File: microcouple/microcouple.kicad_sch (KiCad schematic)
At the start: 1 part, among them P1 USB_C_Plug

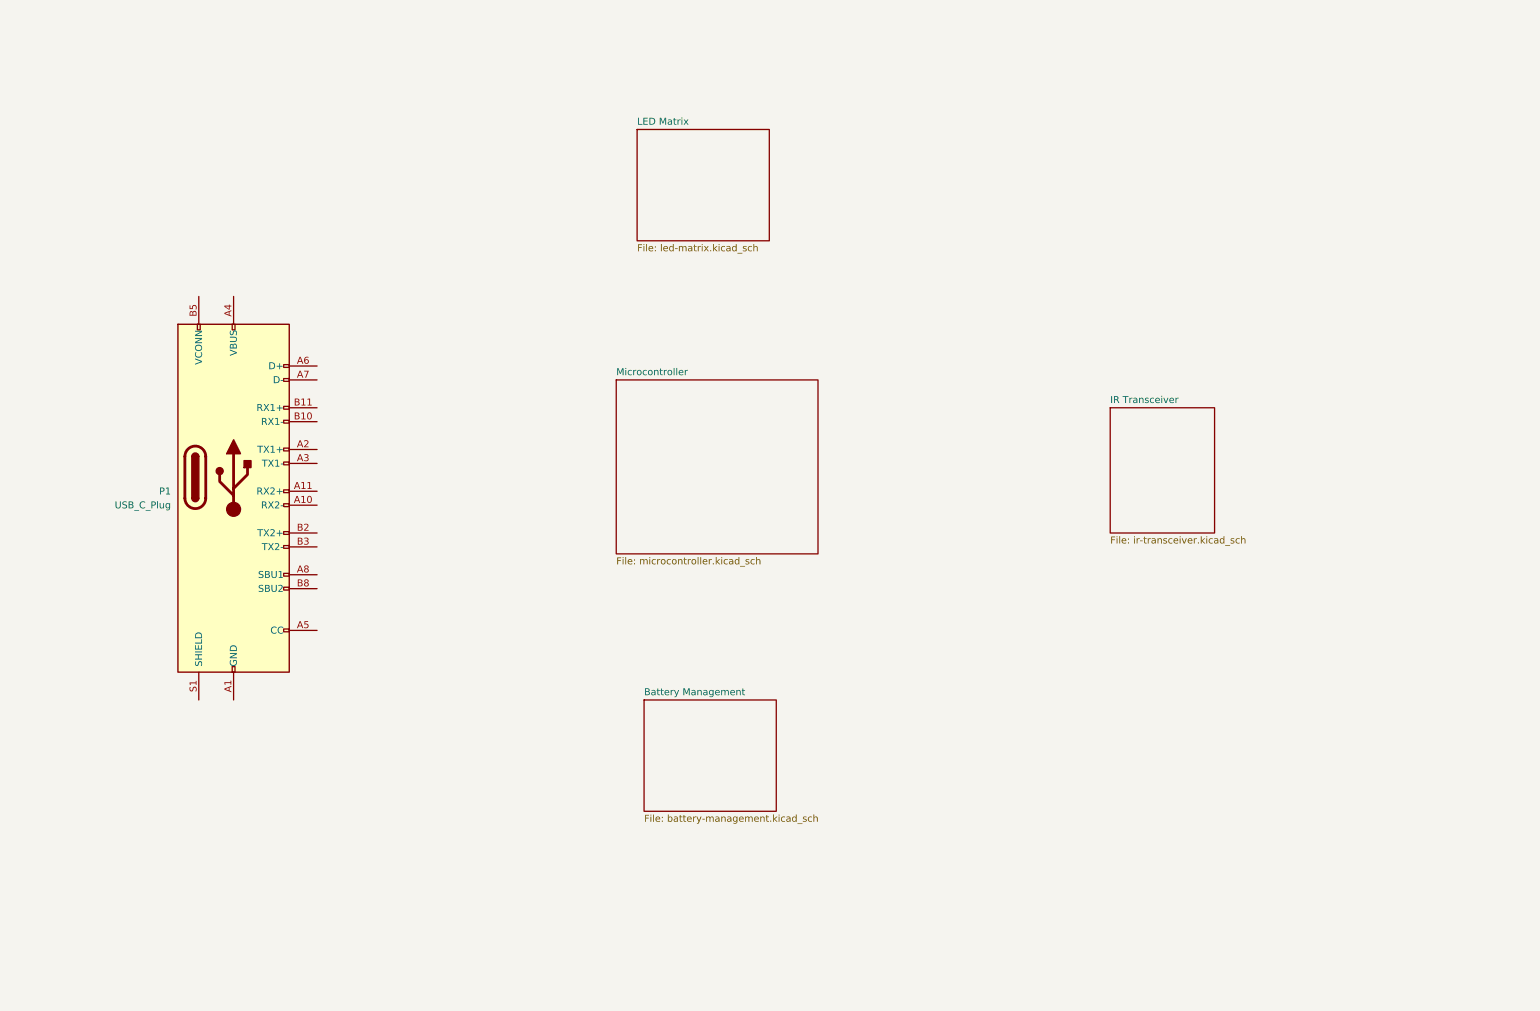
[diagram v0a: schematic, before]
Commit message: Add decoupling caps on MCU
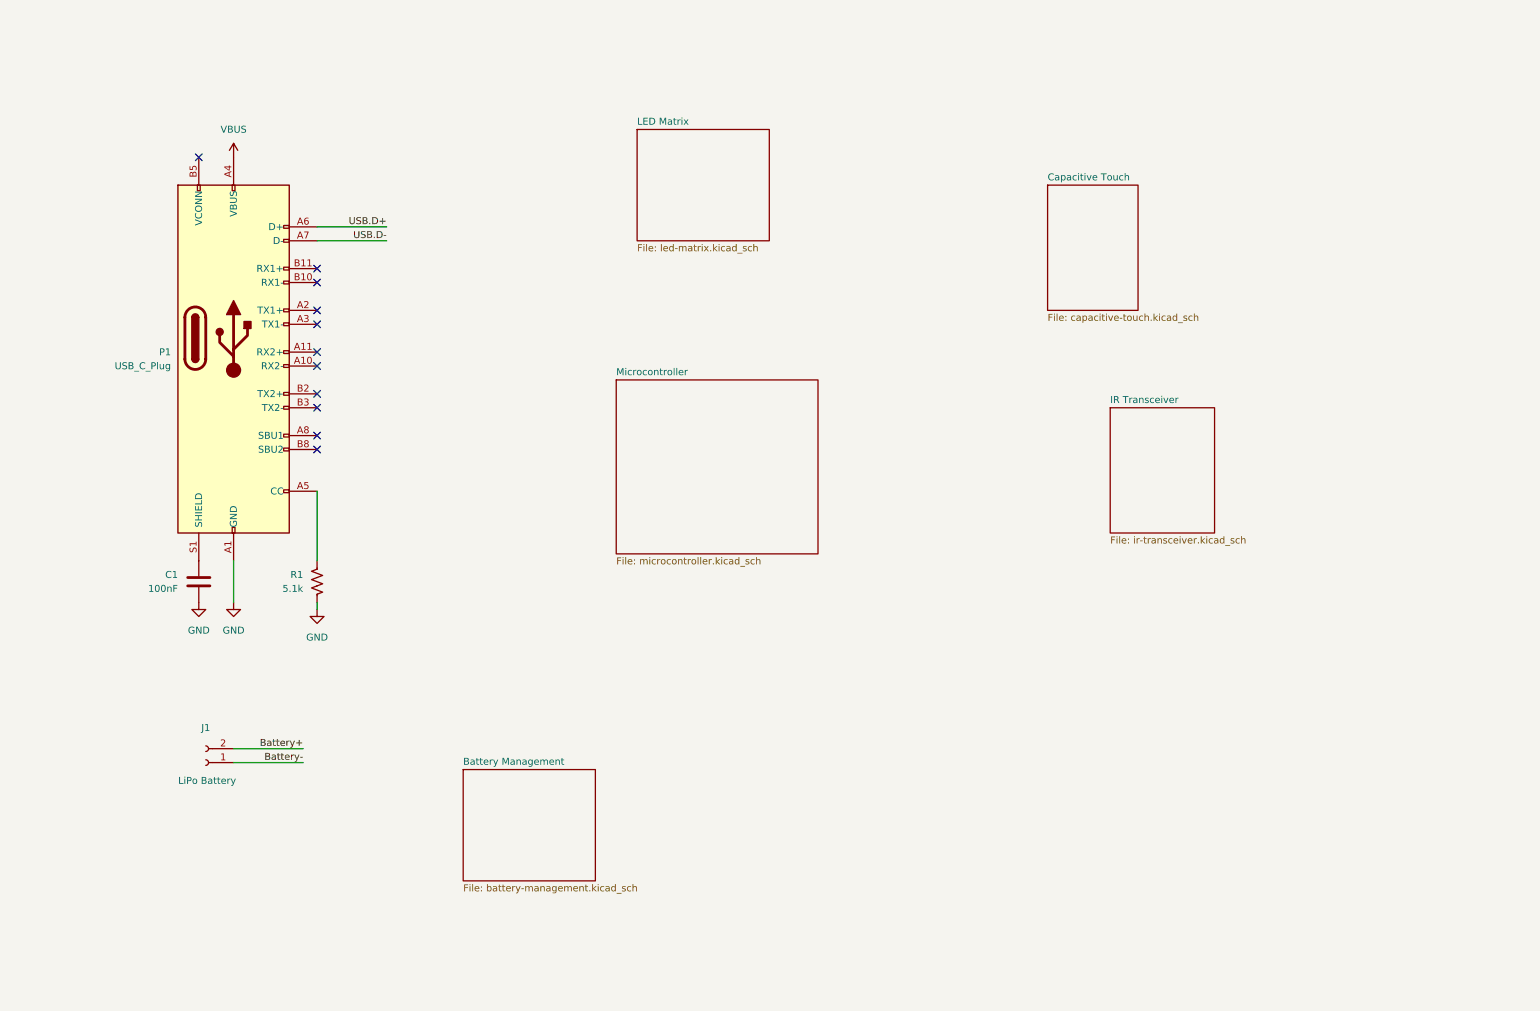
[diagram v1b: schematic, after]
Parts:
- added C1: 100nF, Capacitor_SMD:C_0805_2012Metric, symbol Device:C
- added J1: LiPo Battery, Connector_JST:JST_PH_S2B-PH-K_1x02_P2.00mm_Horizontal, symbol Connector:Conn_01x02_Socket
- added R1: 5.1k, Resistor_SMD:R_0805_2012Metric_Pad1.20x1.40mm_HandSolder, symbol Device:R_US
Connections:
- net GND: now reaches P1.A1 (GND), P1.A12 (GND), P1.B1 (GND), P1.B12 (GND)
- net GND: now also C1.2, R1.2
- net VBUS: now reaches P1.A4 (VBUS), P1.A9 (VBUS), P1.B4 (VBUS), P1.B9 (VBUS)
- net at P1.A5 (CC): now also R1.1
- net USB.D+: now reaches P1.A6 (D+)
- net USB.D-: now reaches P1.A7 (D-)
- net at P1.S1 (SHIELD): now also C1.1
- new net Battery+: J1.2 (Pin_2)
- new net Battery-: J1.1 (Pin_1)
- no-connect marks 0 -> 11
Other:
- added sheet Capacitive Touch (capacitive-touch.kicad_sch)
- moved on the sheet: P1

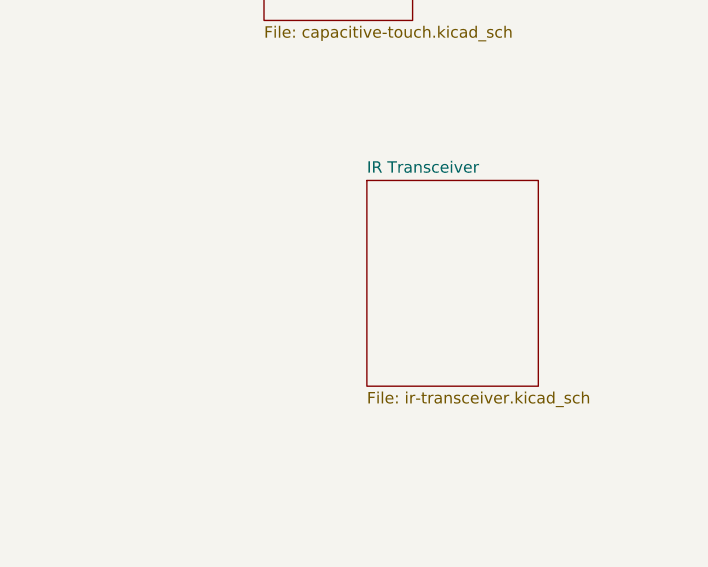
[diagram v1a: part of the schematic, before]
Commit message: Sketch out LED matrix
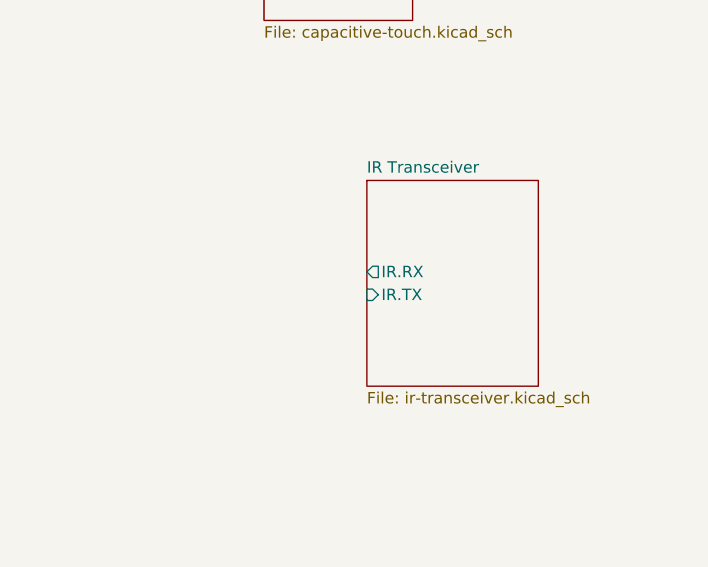
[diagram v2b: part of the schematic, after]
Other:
- sheet IR Transceiver ports: added IR.RX, IR.TX; removed none
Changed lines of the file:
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@@
+			)
+		)
+		(pin "IR.RX" output
+			(at 213.36 96.52 180)
+			(effects
+				(font
+					(size 1.27 1.27)
+				)
+				(justify left)
+			)
+		)
+		(pin "IR.TX" input
+			(at 213.36 99.06 180)
+			(effects
+				(font
+					(size 1.27 1.27)
+				)
+				(justify left)
 			)
 		)

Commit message: Finalize battery management
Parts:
- removed J1: LiPo Battery, Connector_JST:JST_PH_S2B-PH-K_1x02_P2.00mm_Horizontal, symbol Connector:Conn_01x02_Socket
- added BT1: 3.7V Lipo battery, Connector_JST:JST_PH_S2B-PH-K_1x02_P2.00mm_Horizontal, symbol Device:Battery_Cell
- added C15, C8, C9: 4.7uF, Capacitor_SMD:C_0805_2012Metric_Pad1.18x1.45mm_HandSolder, symbol Device:C
- added C2, C3, C4, C5, C6, C7: 100nF, Capacitor_SMD:C_0805_2012Metric_Pad1.18x1.45mm_HandSolder, symbol Device:C
- added D69: IR, LED_THT:LED_D5.0mm_Horizontal_O1.27mm_Z3.0mm_Clear, symbol Device:LED
- added FB1: 120R @ 100MHz, Inductor_SMD:L_0805_2012Metric_Pad1.15x1.40mm_HandSolder, symbol Device:FerriteBead
- added R7: 180R, Resistor_SMD:R_0805_2012Metric_Pad1.20x1.40mm_HandSolder, symbol Device:R_US
- added U1: RP2040, Package_DFN_QFN:QFN-56-1EP_7x7mm_P0.4mm_EP3.2x3.2mm, symbol MCU_RaspberryPi:RP2040
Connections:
- net GND: now also BT1.2 (-), C15.2, C2.2, C4.2, C5.2, C6.2, C7.2, C8.2, C9.2, U1.57 (GND)
- net VBUS: now also C15.1
- new net: U1.1 (IOVDD), U1.10 (IOVDD), U1.22 (IOVDD), U1.33 (IOVDD), U1.42 (IOVDD), U1.49 (IOVDD)
- new net: U1.23 (DVDD), U1.50 (DVDD)
- new net +3.3V: C2.1, C3.1, C4.1, C5.1, C6.1, C8.1, FB1.1
- new net +3.3VA: C7.1, C9.1, FB1.2
- new net Battery Management/BATT+: BT1.1 (+)
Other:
- removed sheet Microcontroller
- sheet Battery Management ports: added +3.3V, BATT+, VBUS; removed none
- note added: "Modulated at 38kHz NEC transmission protocol"
- moved on the sheet: C1, P1, R1

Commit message: Finish base MCU design
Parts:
- added C10: 100nF, Capacitor_SMD:C_0805_2012Metric_Pad1.18x1.45mm_HandSolder, symbol Device:C
- added C11: 4.7uF, Capacitor_SMD:C_0805_2012Metric_Pad1.18x1.45mm_HandSolder, symbol Device:C
- added J1: Conn_ARM_SWD_TagConnect_TC2030-NL, Connector:Tag-Connect_TC2030-IDC-NL_2x03_P1.27mm_Vertical, symbol Connector:Conn_ARM_SWD_TagConnect_TC2030-NL
- added R2: 5.1k, Resistor_SMD:R_0805_2012Metric_Pad1.20x1.40mm_HandSolder, symbol Device:R_US
- added SW1: ~{RESET}, Button_Switch_SMD:SW_SPST_PTS810, symbol Switch:SW_Push
- added X1: 12 MHz 12 pF, Crystal:Crystal_SMD_3225-4Pin_3.2x2.5mm_HandSoldering, symbol Device:Crystal_GND24
- BT1: value 3.7V Lipo battery -> 3.7 V LiPo
- C2, C3: value 100nF -> 14 pF
- P1: footprint GS_Connectors:USB-C-SMD -> (none)
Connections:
- net +3.3V: now also U1.1 (IOVDD), U1.10 (IOVDD), U1.22 (IOVDD), U1.33 (IOVDD), U1.42 (IOVDD), U1.44 (VREG_IN), U1.48 (USB_VDD), U1.49 (IOVDD), J1.1 (VCC), R2.1; no longer C2.1, C3.1
- net +3.3VA: now also U1.43 (ADC_AVDD)
- net GND: now also C3.2, U1.19 (TESTEN), C10.2, C11.2, J1.5 (GND), SW1.1, X1.2, X1.4
- net USB.D+: now also U1.47 (USB_DP)
- net USB.D-: now also U1.46 (USB_DM)
- net XIN: now reaches U1.20 (XIN)
- net XIN: now also C3.1, X1.1
- net XOUT: now reaches U1.21 (XOUT)
- net XOUT: now also C2.1, X1.3
- net +1V1: now reaches U1.23 (DVDD), U1.50 (DVDD)
- net +1V1: now also U1.45 (VREG_VOUT), C10.1, C11.1
- net SWCLK: now reaches U1.24 (SWCLK)
- net SWCLK: now also J1.4 (SWCLK)
- net SWDIO: now reaches U1.25 (SWD)
- net SWDIO: now also J1.2 (SWDIO)
- net ~{RESET}: now reaches U1.26 (RUN)
- net ~{RESET}: now also J1.3 (~{RESET}), R2.2, SW1.2
- no-connect marks 11 -> 12
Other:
- removed sheet IR Transceiver
- moved on the sheet: BT1, C1, C15, C4, C5, C6, C7, C8, C9, D69, FB1, P1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

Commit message: Preliminary Schematic
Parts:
- removed R7: 180R, Resistor_SMD:R_0805_2012Metric_Pad1.20x1.40mm_HandSolder, symbol Device:R_US
- added R10, R9: 5.1k, Resistor_SMD:R_0201_0603Metric, symbol Device:R_US
- added R15, R16: 27R, Resistor_SMD:R_0201_0603Metric, symbol Device:R_US
- added R8: 1k, Resistor_SMD:R_0201_0603Metric, symbol Device:R_US
- added U7: USBLC6-2SC6, Package_TO_SOT_SMD:SOT-23-6, symbol Power_Protection:USBLC6-2SC6
- BT1: value 3.7 V LiPo -> 3.7V LiPo
- C1: renamed from C8; footprint Capacitor_SMD:C_0805_2012Metric_Pad1.18x1.45mm_HandSolder -> Capacitor_SMD:C_0402_1005Metric
- C10: renamed from C3; footprint Capacitor_SMD:C_0805_2012Metric_Pad1.18x1.45mm_HandSolder -> Capacitor_SMD:C_0201_0603Metric
- C11: renamed from C2; footprint Capacitor_SMD:C_0805_2012Metric_Pad1.18x1.45mm_HandSolder -> Capacitor_SMD:C_0201_0603Metric
- C12: renamed from C1; footprint Capacitor_SMD:C_0805_2012Metric -> Capacitor_SMD:C_0201_0603Metric
- C2: renamed from C4; footprint Capacitor_SMD:C_0805_2012Metric_Pad1.18x1.45mm_HandSolder -> Capacitor_SMD:C_0201_0603Metric
- C3: renamed from C5; footprint Capacitor_SMD:C_0805_2012Metric_Pad1.18x1.45mm_HandSolder -> Capacitor_SMD:C_0201_0603Metric
- C4: renamed from C6; footprint Capacitor_SMD:C_0805_2012Metric_Pad1.18x1.45mm_HandSolder -> Capacitor_SMD:C_0201_0603Metric
- C5: renamed from C9; footprint Capacitor_SMD:C_0805_2012Metric_Pad1.18x1.45mm_HandSolder -> Capacitor_SMD:C_0402_1005Metric
- C6: renamed from C7; footprint Capacitor_SMD:C_0805_2012Metric_Pad1.18x1.45mm_HandSolder -> Capacitor_SMD:C_0201_0603Metric
- C7: renamed from C11; footprint Capacitor_SMD:C_0805_2012Metric_Pad1.18x1.45mm_HandSolder -> Capacitor_SMD:C_0402_1005Metric
- C8: renamed from C10; footprint Capacitor_SMD:C_0805_2012Metric_Pad1.18x1.45mm_HandSolder -> Capacitor_SMD:C_0201_0603Metric
- C9: renamed from C15; footprint Capacitor_SMD:C_0805_2012Metric_Pad1.18x1.45mm_HandSolder -> Capacitor_SMD:C_0402_1005Metric
- D69: value IR -> GREEN; footprint LED_THT:LED_D5.0mm_Horizontal_O1.27mm_Z3.0mm_Clear -> LED_SMD:LED_0201_0603Metric
- P1: footprint (none) -> GS_Connectors:USB-C-SMD
- R1: renamed from R2; footprint Resistor_SMD:R_0805_2012Metric_Pad1.20x1.40mm_HandSolder -> Resistor_SMD:R_0201_0603Metric
- R3: renamed from R1; footprint Resistor_SMD:R_0805_2012Metric_Pad1.20x1.40mm_HandSolder -> Resistor_SMD:R_0201_0603Metric
- X1: value 12 MHz 12 pF -> 12MHz 12pF
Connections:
- net +3.3V: now also D69.2 (A), R10.1, R9.1
- net GND: now also R8.2, U7.2 (GND)
- net USB.D+: now also U7.1 (I/O1); no longer U1.47 (USB_DP)
- net USB.D-: now also U7.3 (I/O2); no longer U1.46 (USB_DM)
- net VBUS: now also U7.5 (VBUS)
- net I2C0.SDA: now reaches U1.2 (GPIO0)
- net I2C0.SDA: now also R9.2
- net ~{MX_SDB}: now reaches U1.27 (GPIO16)
- net I2C0.SDL: now reaches U1.3 (GPIO1)
- net I2C0.SDL: now also R10.2
- net IR.TX: now reaches U1.37 (GPIO25)
- net IR.RX: now reaches U1.38 (GPIO26_ADC0)
- net CT_RESET: now reaches U1.5 (GPIO3)
- net CT_WAKE: now reaches U1.6 (GPIO4)
- net ~{CT_ALERT}: now reaches U1.7 (GPIO5)
- net at D69.1 (K): now also R8.1
- net Battery Management/BATT+ renamed +BATT
- new net: R16.2, U1.46 (USB_DM)
- new net: R15.2, U1.47 (USB_DP)
- new net USB.D_PROTECTED+: R15.1, U7.6 (I/O1)
- new net USB.D_PROTECTED-: R16.1, U7.4 (I/O2)
- no-connect marks 12 -> 40
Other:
- added sheet IR Transciever (ir-transciever.kicad_sch)
- sheet Battery Management ports: added +BATT; removed BATT+
- sheet Capacitive Touch ports: added CT_RESET, CT_WAKE, I2C.SCL, I2C.SDA, ~{CT_ALERT}; removed none
- sheet LED Matrix ports: added I2C.SCL, I2C.SDA, ~{MX_SDB}; removed none
- note removed: "Modulated at 38kHz NEC transmission protocol"
- company: (none) -> George Sleen
- moved on the sheet: BT1, C1, C2, C3, C4, C5, C6, C7, C8, C9, FB1, R1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

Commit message: Switch THT IR components to SMD ones
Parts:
- P1: LCSC ID C2835315 -> C2681555
- U2: renamed from U1; symbol MCU_RaspberryPi:RP2040 -> GS_MCU:RP2040
- X1: footprint Crystal:Crystal_SMD_3225-4Pin_3.2x2.5mm_HandSoldering -> Crystal:Crystal_SMD_3225-4Pin_3.2x2.5mm
- renumbered C4 to C1, C3 to C2, C2 to C3, C1 to C4, D69 to D1, R8 to R1, R1 to R2, R10 to R3, R9 to R4, R15 to R5, R16 to R6, R3 to R7, U7 to U1
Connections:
- net USB.D+: now also P1.B6 (D+)
- net USB.D-: now also P1.B7 (D-)
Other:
- moved on the sheet: BT1, C12, C9, D1, P1, R1, R2, R5, R6, R7, SW1, U1

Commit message: Fix faulty USB-C CC pin connections
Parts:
- added R17: 5.1k, Resistor_SMD:R_0201_0603Metric, symbol Device:R_US
- J1: renamed from P1; value USB_C_Plug -> USB_C_Socket; symbol GS_Connectors:USB_C_Plug -> GS_Connectors:USB_C_Socket
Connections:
- net GND: now also R17.1
- net USB.D_PROTECTED-: now also R6.2; no longer R6.1
- net at U2.46 (USB_DM): now also R6.1; no longer R6.2
- net at J1.A5 (CC1): now also R17.2; no longer R7.1
- net at J1.B5 (CC2): now also R7.1
- no-connect marks 40 -> 39
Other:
- moved on the sheet: R6
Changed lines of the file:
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@@
 	)
 	(no_connect
-		(at 39.37 66.04)
-	)
-	(no_connect
 		(at 185.42 121.92)
 	)
@@
 	(wire
 		(pts
+			(xy 67.31 139.7) (xy 67.31 124.46)
+		)
+		(stroke
+			(width 0)
+			(type default)
+		)
+	)
+	(wire
+		(pts
+			(xy 67.31 124.46) (xy 60.96 124.46)
+		)
+		(stroke
+			(width 0)
+			(type default)
+		)
+	)
+	(wire
+		(pts
 			(xy 92.71 116.84) (xy 85.09 116.84)
 		)
@@
 	(wire
 		(pts
+			(xy 67.31 148.59) (xy 67.31 147.32)
+		)
+		(stroke
+			(width 0)
+			(type default)
+		)
+	)
+	(wire
+		(pts
 			(xy 83.82 81.28) (xy 115.57 81.28)
 		)
@@
 	)
 	(symbol
+		(lib_id "Device:R_US")
+		(at 67.31 143.51 0)
+		(mirror x)
+		(unit 1)
+		(exclude_from_sim no)
+		(in_bom yes)
+		(on_board yes)
+		(dnp no)
+		(property "Reference" "R17"
+			(at 69.85 144.7801 0)
+			(effects
+				(font
+					(size 1.27 1.27)
+				)
+				(justify left)
+			)
+		)
+		(property "Value" "5.1k"
+			(at 69.85 142.2401 0)
+			(effects
+				(font
+					(size 1.27 1.27)
+				)
+				(justify left)
+			)
+		)
+		(property "Footprint" "Resistor_SMD:R_0201_0603Metric"
+			(at 68.326 143.256 90)
+			(effects
+				(font
+					(size 1.27 1.27)
+				)
+				(hide yes)
+			)
+		)
+		(property "Datasheet" "~"
+			(at 67.31 143.51 0)
+			(effects
+				(font
+					(size 1.27 1.27)
+				)
+				(hide yes)
+			)
+		)
+		(property "Description" "Resistor, US symbol"
+			(at 67.31 143.51 0)
+			(effects
+				(font
+					(size 1.27 1.27)
+				)
+				(hide yes)
+			)
+		)
+		(pin "1"
+		)
+		(pin "2"
+		)
+		(instances
+			(project "microcouple"
+				(path "/d639f16d-aedb-4af6-af94-94ea25244267"
+					(reference "R17")
+					(unit 1)
+				)
+			)
+		)
+	)
+	(symbol
 		(lib_id "Device:C")
 		(at 218.44 33.02 0)
@@
 	)
 	(symbol
-		(lib_id "GS_Connectors:USB_C_Plug")
+		(lib_id "GS_Connectors:USB_C_Socket")
 		(at 45.72 99.06 0)
 		(unit 1)
@@
 		(dnp no)
 		(fields_autoplaced yes)
-		(property "Reference" "P1"
+		(property "Reference" "J1"
 			(at 34.29 101.5999 0)
 			(effects
@@
 			)
 		)
-		(property "Value" "USB_C_Plug"
+		(property "Value" "USB_C_Socket"
 			(at 34.29 104.1399 0)
 			(effects
@@
 		)
 		(property "Footprint" "GS_Connectors:USB-C-SMD"
-			(at 49.53 100.33 0)
+			(at 45.72 53.34 0)
 			(effects
 				(font
@@
 			)
 		)
-		(property "Description" "USB Type-C Plug connector"
+		(property "Description" "USB Type-C Socket connector"
 			(at 46.228 45.466 0)
 			(effects
@@
 		)
 		(property "LCSC ID" "C2681555"
-			(at 45.72 99.06 0)
+			(at 45.72 51.054 0)
 			(effects
 				(font
@@
 			(project ""
 				(path "/d639f16d-aedb-4af6-af94-94ea25244267"
-					(reference "P1")
+					(reference "J1")
 					(unit 1)
 				)
@@
 	)
 	(symbol
+		(lib_id "power:GND")
+		(at 67.31 148.59 0)
+		(unit 1)
+		(exclude_from_sim no)
+		(in_bom yes)
+		(on_board yes)
+		(dnp no)
+		(property "Reference" "#PWR079"
+			(at 67.31 154.94 0)
+			(effects
+				(font
+					(size 1.27 1.27)
+				)
+				(hide yes)
+			)
+		)
+		(property "Value" "GND"
+			(at 67.31 153.67 0)
+			(effects
+				(font
+					(size 1.27 1.27)
+				)
+			)
+		)
+		(property "Footprint" ""
+			(at 67.31 148.59 0)
+			(effects
+				(font
+					(size 1.27 1.27)
+				)
+				(hide yes)
+			)
+		)
+		(property "Datasheet" ""
+			(at 67.31 148.59 0)
+			(effects
+				(font
+					(size 1.27 1.27)
+				)
+				(hide yes)
+			)
+		)
+		(property "Description" "Power symbol creates a global label with name \"GND\" , ground"
+			(at 67.31 148.59 0)
+			(effects
+				(font
+					(size 1.27 1.27)
+				)
+				(hide yes)
+			)
+		)
+		(pin "1"
+		)
+		(instances
+			(project "microcouple"
+				(path "/d639f16d-aedb-4af6-af94-94ea25244267"
+					(reference "#PWR079")
+					(unit 1)
+				)
+			)
+		)
+	)
+	(symbol
 		(lib_id "Device:C")
 		(at 269.24 33.02 0)
@@
 	(symbol
 		(lib_id "Device:R_US")
-		(at 119.38 81.28 90)
-		(mirror x)
+		(at 119.38 81.28 270)
 		(unit 1)
 		(exclude_from_sim no)
@@
 		)
 		(property "Footprint" "Resistor_SMD:R_0201_0603Metric"
-			(at 119.634 82.296 90)
+			(at 119.126 82.296 90)
 			(effects
 				(font

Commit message: Draft layout
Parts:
- removed R5, R6: 27R, Resistor_SMD:R_0201_0603Metric, symbol Device:R_US
- added C19, C24, C25, C26: 100nF, Capacitor_SMD:C_0201_0603Metric, symbol Device:C
- added H1, H2, H3: MountingHole_Pad, MountingHole:MountingHole_2.2mm_M2_DIN965_Pad, symbol Mechanical:MountingHole_Pad
- BT1: footprint Connector_JST:JST_PH_S2B-PH-K_1x02_P2.00mm_Horizontal -> Connector_PinSocket_1.27mm:PinSocket_2x01_P1.27mm_Vertical; now not fitted
- SW1: footprint Button_Switch_SMD:SW_SPST_PTS810 -> Button_Switch_SMD:SW_SPST_B3U-1000P; LCSC ID C115360 -> (none)
- renumbered C9 to C1, C6 to C10, C7 to C11, C8 to C12, C12 to C2, C10 to C3, C11 to C4, C1 to C5, C2 to C6, C3 to C7, C4 to C8, C5 to C9, J1 to J2, R7 to R1, R17 to R2, R1 to R3, R2 to R6, R3 to R7, R4 to R8
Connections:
- net +3.3V: now also C19.1
- net GND: now also C19.2, C24.2, C25.2, C26.2
- net USB.D_PROTECTED+: now also U2.47 (USB_DP)
- net USB.D_PROTECTED-: now also U2.46 (USB_DM)
- new net: C26.1, H3.1
- new net: C24.1, H1.1
- new net: C25.1, H2.1
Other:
- title: (none) -> Microcouple
- moved on the sheet: C5, C6, C7, C8
